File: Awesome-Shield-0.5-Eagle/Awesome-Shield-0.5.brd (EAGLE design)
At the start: 100 x 80 mm, 24 parts, among them J1 ARDUINO_R3_SHIELDUNO_R3_SHIEL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, SW1 SPST_TACT-EVQQ2

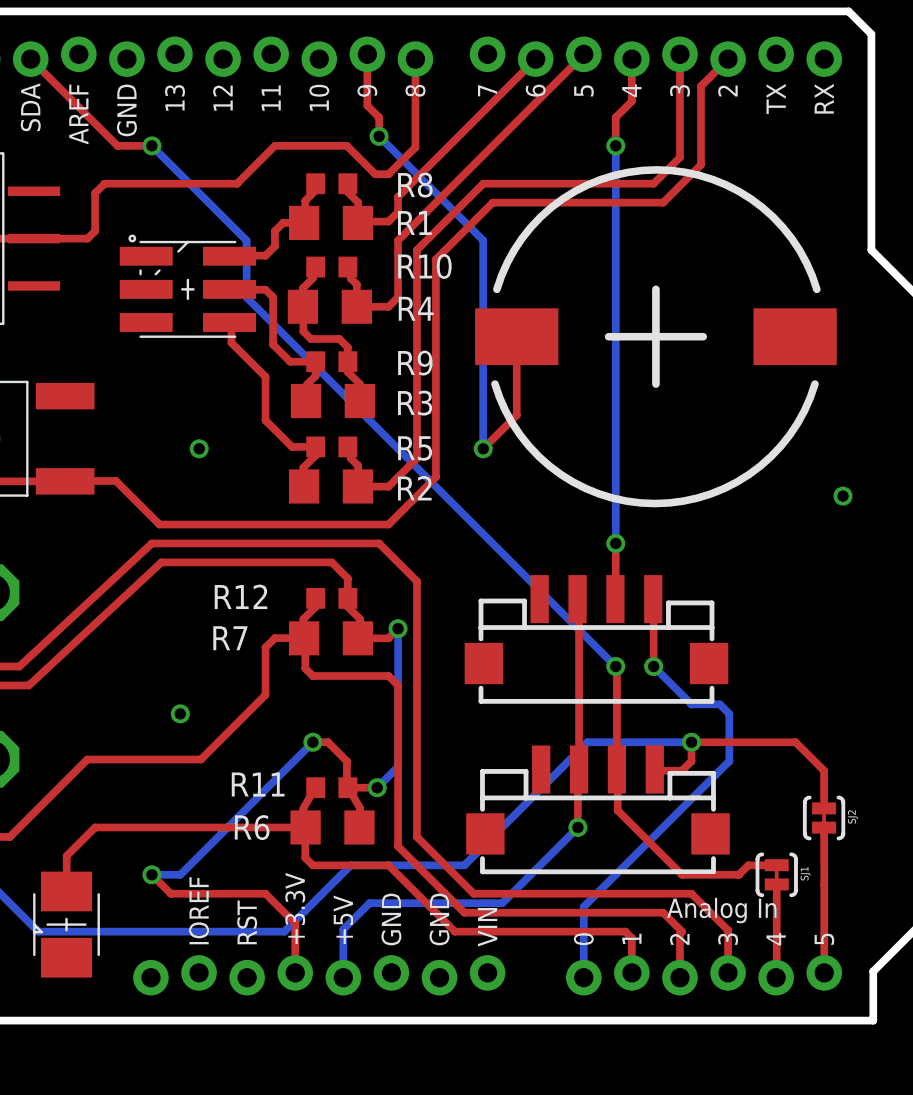
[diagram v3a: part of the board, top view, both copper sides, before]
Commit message: gave vias more space around them
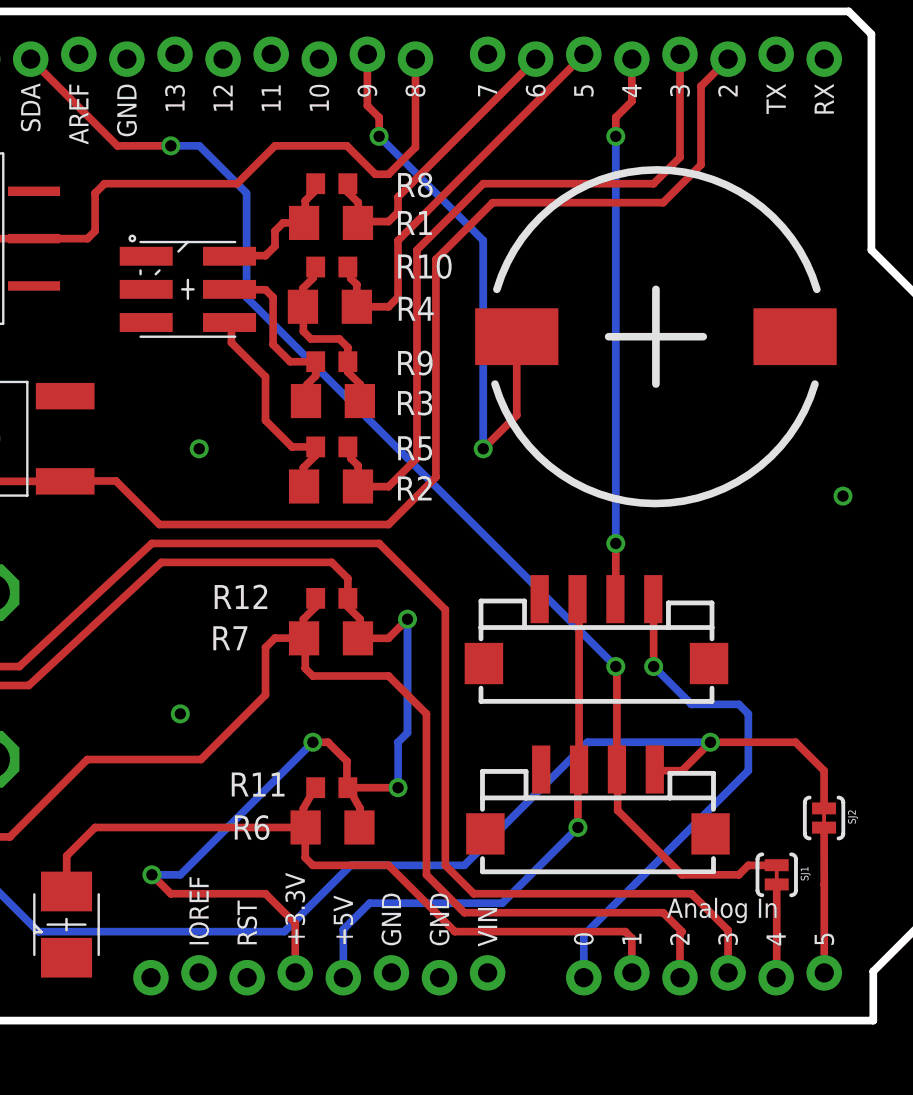
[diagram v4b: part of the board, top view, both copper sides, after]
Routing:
- net +3V3: track 74.5 -> 76.6 mm
- net SDA: track 63.6 -> 65.1 mm
- net A0: track 25.7 -> 27.1 mm
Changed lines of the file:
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@@
 <wire x1="55.5" y1="38.108" x2="55.382" y2="37.99" width="0.4064" layer="1"/>
 <wire x1="55.382" y1="37.99" x2="56.99" y2="37.99" width="0.4064" layer="1"/>
-<wire x1="56.99" y1="37.99" x2="57.5" y2="38.5" width="0.4064" layer="1"/>
-<via x="57.5" y="38.5" extent="1-16" drill="0.6" shape="square"/>
-<wire x1="57.5" y1="38.5" x2="57.5" y2="31.2" width="0.4064" layer="16"/>
-<wire x1="57.5" y1="31.2" x2="56.4" y2="30.1" width="0.4064" layer="16"/>
-<via x="56.4" y="30.1" extent="1-16" drill="0.6" shape="square"/>
-<wire x1="56.4" y1="30.1" x2="54.85" y2="30.1" width="0.4064" layer="1"/>
+<wire x1="56.99" y1="37.99" x2="58" y2="39" width="0.4064" layer="1"/>
+<via x="58" y="39" extent="1-16" drill="0.6" shape="square"/>
+<via x="57.5" y="30.1" extent="1-16" drill="0.6" shape="square"/>
+<wire x1="57.5" y1="30.1" x2="54.85" y2="30.1" width="0.4064" layer="1"/>
 <wire x1="54.85" y1="40.1" x2="54.85" y2="41.15" width="0.4064" layer="1"/>
 <wire x1="54.85" y1="41.15" x2="54" y2="42" width="0.4064" layer="1"/>
@@
 <wire x1="54.8" y1="31.5" x2="54.8" y2="30.05" width="0.4064" layer="1"/>
 <wire x1="54.8" y1="30.05" x2="54.85" y2="30.1" width="0.4064" layer="1"/>
+<wire x1="58" y1="39" x2="58" y2="33" width="0.4064" layer="16"/>
+<wire x1="58" y1="33" x2="57.5" y2="32.5" width="0.4064" layer="16"/>
+<wire x1="57.5" y1="32.5" x2="57.5" y2="30.1" width="0.4064" layer="16"/>
 </signal>
 <signal name="A1">
@@
 <wire x1="72.5" y1="22.5" x2="71.5" y2="23.5" width="0.4064" layer="1"/>
 <wire x1="71.5" y1="23.5" x2="61" y2="23.5" width="0.4064" layer="1"/>
-<wire x1="61" y1="23.5" x2="57.5" y2="27" width="0.4064" layer="1"/>
 <wire x1="52.6" y1="36.4" x2="52.6" y2="37.928" width="0.4064" layer="1"/>
 <wire x1="52.6" y1="37.928" x2="52.538" y2="37.99" width="0.4064" layer="1"/>
@@
 <wire x1="52.6" y1="36.4" x2="53" y2="36" width="0.4064" layer="1"/>
 <wire x1="53" y1="36" x2="57" y2="36" width="0.4064" layer="1"/>
-<wire x1="57" y1="36" x2="57.5" y2="35.5" width="0.4064" layer="1"/>
-<wire x1="57.5" y1="35.5" x2="57.5" y2="27" width="0.4064" layer="1"/>
 <wire x1="47.09" y1="31.59" x2="41.09" y2="31.59" width="0.4064" layer="1"/>
 <wire x1="41.09" y1="31.59" x2="37" y2="27.5" width="0.4064" layer="1"/>
@@
 <wire x1="31.5" y1="27" x2="31.5" y2="24.845" width="0.4064" layer="1"/>
 <wire x1="31.5" y1="24.845" x2="31.41" y2="24.755" width="0.4064" layer="1"/>
+<wire x1="61" y1="23.5" x2="59" y2="25.5" width="0.4064" layer="1"/>
+<wire x1="59" y1="25.5" x2="59" y2="34" width="0.4064" layer="1"/>
+<wire x1="59" y1="34" x2="57" y2="36" width="0.4064" layer="1"/>
 </signal>
 <signal name="N$3">
@@
 <contactref element="J2" pad="1"/>
 <contactref element="J1" pad="A0"/>
-<wire x1="67.31" y1="20.066" x2="67.31" y2="23.81" width="0.4064" layer="16"/>
-<wire x1="67.31" y1="23.81" x2="75" y2="31.5" width="0.4064" layer="16"/>
-<wire x1="75" y1="31.5" x2="75" y2="34" width="0.4064" layer="16"/>
-<wire x1="75" y1="34" x2="74.5" y2="34.5" width="0.4064" layer="16"/>
-<wire x1="74.5" y1="34.5" x2="73" y2="34.5" width="0.4064" layer="16"/>
+<wire x1="75.5" y1="34.5" x2="73" y2="34.5" width="0.4064" layer="16"/>
 <wire x1="73" y1="34.5" x2="71" y2="36.5" width="0.4064" layer="16"/>
 <via x="71" y="36.5" extent="1-16" drill="0.6" shape="square"/>
 <wire x1="71" y1="36.5" x2="71" y2="40.04" width="0.4064" layer="1"/>
 <wire x1="71" y1="40.04" x2="70.98" y2="40.06" width="0.4064" layer="1"/>
+<wire x1="67.31" y1="20.066" x2="67.31" y2="22.31" width="0.4064" layer="16"/>
+<wire x1="67.31" y1="22.31" x2="76" y2="31" width="0.4064" layer="16"/>
+<wire x1="76" y1="31" x2="76" y2="34" width="0.4064" layer="16"/>
+<wire x1="76" y1="34" x2="75.5" y2="34.5" width="0.4064" layer="16"/>
 </signal>
 <signal name="A5">
@@
 <via x="32.5" y="68.5" extent="1-16" drill="0.6" shape="square"/>
 <wire x1="32.5" y1="68.5" x2="32.5" y2="28.5" width="0.4064" layer="16"/>
-<via x="73" y="32.5" extent="1-16" drill="0.6" shape="square"/>
+<via x="74" y="32.5" extent="1-16" drill="0.6" shape="square"/>
 <wire x1="71" y1="31.12" x2="71.06" y2="31.06" width="0.4064" layer="1"/>
 <wire x1="80" y1="29.008" x2="80" y2="31" width="0.4064" layer="1"/>
 <wire x1="80" y1="31" x2="78.5" y2="32.5" width="0.4064" layer="1"/>
-<wire x1="78.5" y1="32.5" x2="73" y2="32.5" width="0.4064" layer="1"/>
-<wire x1="73" y1="32.5" x2="73" y2="31.5" width="0.4064" layer="1"/>
-<wire x1="73" y1="31.5" x2="72.5" y2="31" width="0.4064" layer="1"/>
+<wire x1="78.5" y1="32.5" x2="74" y2="32.5" width="0.4064" layer="1"/>
+<wire x1="74" y1="32.5" x2="72.5" y2="31" width="0.4064" layer="1"/>
 <wire x1="72.5" y1="31" x2="71.12" y2="31" width="0.4064" layer="1"/>
 <wire x1="71.12" y1="31" x2="71.06" y2="31.06" width="0.4064" layer="1"/>
 <wire x1="67.5" y1="32.5" x2="61" y2="26" width="0.4064" layer="16"/>
 <wire x1="38.5" y1="22.5" x2="32.5" y2="28.5" width="0.4064" layer="16"/>
-<wire x1="73" y1="32.5" x2="67.5" y2="32.5" width="0.4064" layer="16"/>
+<wire x1="74" y1="32.5" x2="67.5" y2="32.5" width="0.4064" layer="16"/>
 <wire x1="38.5" y1="22.5" x2="51.5" y2="22.5" width="0.4064" layer="16"/>
 <wire x1="51.5" y1="22.5" x2="55" y2="26" width="0.4064" layer="16"/>
@@
 <via x="69" y="36.5" extent="1-16" drill="0.6" shape="square"/>
 <wire x1="69" y1="36.5" x2="49.5" y2="56" width="0.4064" layer="16"/>
-<wire x1="49.5" y1="56" x2="49.5" y2="59" width="0.4064" layer="16"/>
-<wire x1="49.5" y1="59" x2="44.5" y2="64" width="0.4064" layer="16"/>
-<via x="44.5" y="64" extent="1-16" drill="0.6" shape="square"/>
-<wire x1="44.5" y1="64" x2="42.68" y2="64" width="0.4064" layer="1"/>
+<wire x1="49.5" y1="56" x2="49.5" y2="61.5" width="0.4064" layer="16"/>
+<via x="45.5" y="64" extent="1-16" drill="0.6" shape="square"/>
+<wire x1="45.5" y1="64" x2="42.68" y2="64" width="0.4064" layer="1"/>
 <wire x1="42.68" y1="64" x2="38.1" y2="68.58" width="0.4064" layer="1"/>
 <wire x1="72.5" y1="25.5" x2="75.5" y2="25.5" width="0.4064" layer="1"/>
@@
 <wire x1="76" y1="26" x2="77.492" y2="26" width="0.4064" layer="1"/>
 <wire x1="77.492" y1="26" x2="77.5" y2="26.008" width="0.4064" layer="1"/>
+<wire x1="49.5" y1="61.5" x2="47" y2="64" width="0.4064" layer="16"/>
+<wire x1="47" y1="64" x2="45.5" y2="64" width="0.4064" layer="16"/>
 </signal>
 <signal name="D8">
@@
 <contactref element="J2" pad="2"/>
 <wire x1="69.85" y1="68.58" x2="69.85" y2="66.35" width="0.4064" layer="1"/>
-<via x="69" y="64" extent="1-16" drill="0.6" shape="square"/>
-<wire x1="69" y1="64" x2="69" y2="43" width="0.4064" layer="16"/>
+<via x="69" y="64.5" extent="1-16" drill="0.6" shape="square"/>
+<wire x1="69" y1="64.5" x2="69" y2="43" width="0.4064" layer="16"/>
 <via x="69" y="43" extent="1-16" drill="0.6" shape="square"/>
 <wire x1="69" y1="43" x2="69" y2="40.08" width="0.4064" layer="1"/>
 <wire x1="69" y1="40.08" x2="68.98" y2="40.06" width="0.4064" layer="1"/>
 <wire x1="69.85" y1="66.35" x2="69" y2="65.5" width="0.4064" layer="1"/>
-<wire x1="69" y1="65.5" x2="69" y2="64" width="0.4064" layer="1"/>
+<wire x1="69" y1="65.5" x2="69" y2="64.5" width="0.4064" layer="1"/>
 </signal>
 <signal name="N$2">
@@
 <wire x1="74.93" y1="22.57" x2="73" y2="24.5" width="0.4064" layer="1"/>
 <wire x1="73" y1="24.5" x2="61.5" y2="24.5" width="0.4064" layer="1"/>
-<wire x1="61.5" y1="24.5" x2="58.5" y2="27.5" width="0.4064" layer="1"/>
-<wire x1="58.5" y1="27.5" x2="58.5" y2="41" width="0.4064" layer="1"/>
-<wire x1="58.5" y1="41" x2="56.5" y2="43" width="0.4064" layer="1"/>
+<wire x1="60" y1="39.5" x2="56.5" y2="43" width="0.4064" layer="1"/>
 <wire x1="56.5" y1="43" x2="44.5" y2="43" width="0.4064" layer="1"/>
 <wire x1="44.5" y1="43" x2="37.5" y2="36.5" width="0.4064" layer="1"/>
@@
 <wire x1="33" y1="36.5" x2="31" y2="38.5" width="0.4064" layer="1"/>
 <wire x1="31" y1="38.5" x2="29" y2="38.5" width="0.4064" layer="1"/>
+<wire x1="61.5" y1="24.5" x2="60" y2="26" width="0.4064" layer="1"/>
+<wire x1="60" y1="26" x2="60" y2="39.5" width="0.4064" layer="1"/>
 </signal>
 </signals>

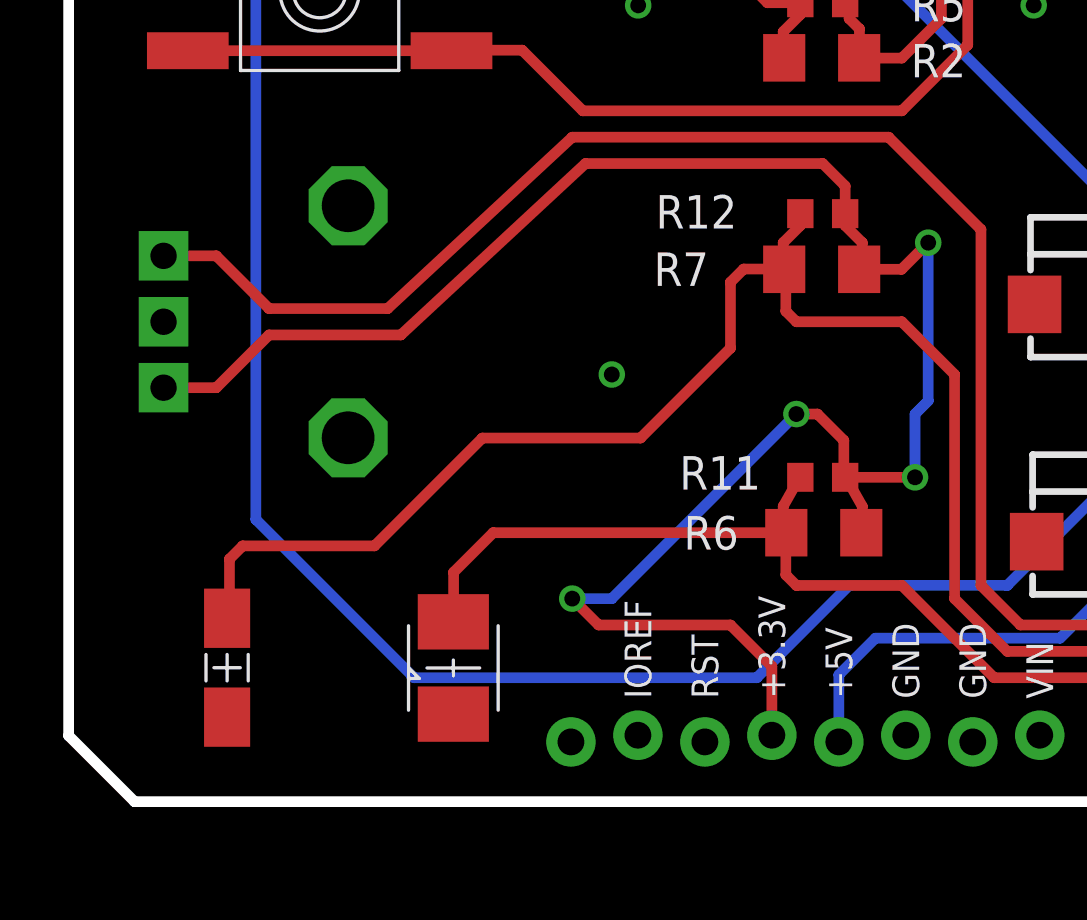
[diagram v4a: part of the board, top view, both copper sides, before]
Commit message: changed vias to round, powered potentiometer from IOREF instead of +3V3 power rail, trace and via tweaks
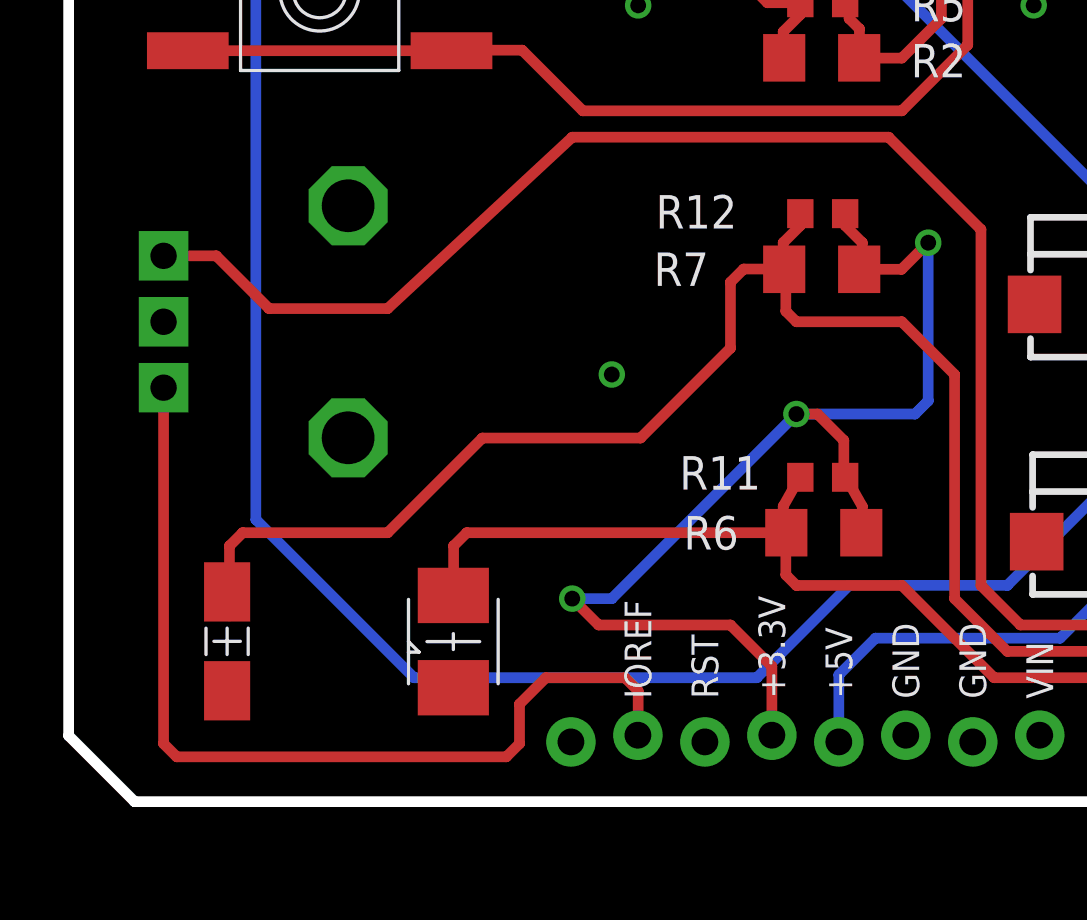
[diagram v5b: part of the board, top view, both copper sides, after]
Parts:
- moved F1 1.00 mm to (31.4, 23.9)
- moved Q1 1.00 mm to (40.0, 23.9)
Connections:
- new net IOREF: J1.IOREF, RV1.P$3
- net +3V3: no longer RV1.P$3
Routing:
- net IOREF: track 0.00 -> 35.7 mm
- net +3V3: track 76.6 -> 45.4 mm, vias 4 -> 3
- net A2: track 66.5 -> 67.1 mm
